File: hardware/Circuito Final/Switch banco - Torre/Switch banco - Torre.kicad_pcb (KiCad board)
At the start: 2 copper layers, 98.6 x 49 mm, 60 parts, among them J1 Conn_01x07, J2 Conn_02x07_Odd_Even, J3 Conn_01x07, Q1 MMBFJ112, Q1_1 MMBT2222A, Q3 MMBT2222A, U1 74HC595, U2 74HC4051

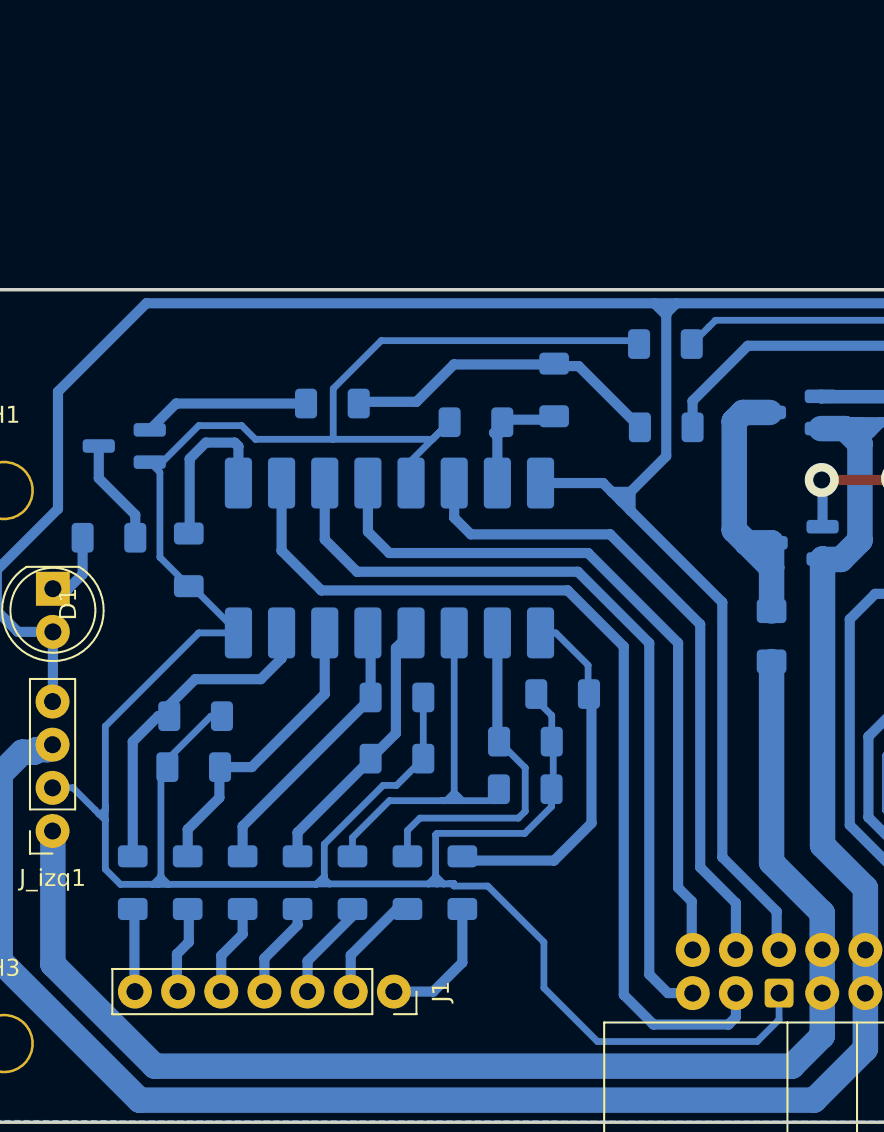
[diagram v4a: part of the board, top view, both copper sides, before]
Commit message: comienza arreglo de huellas
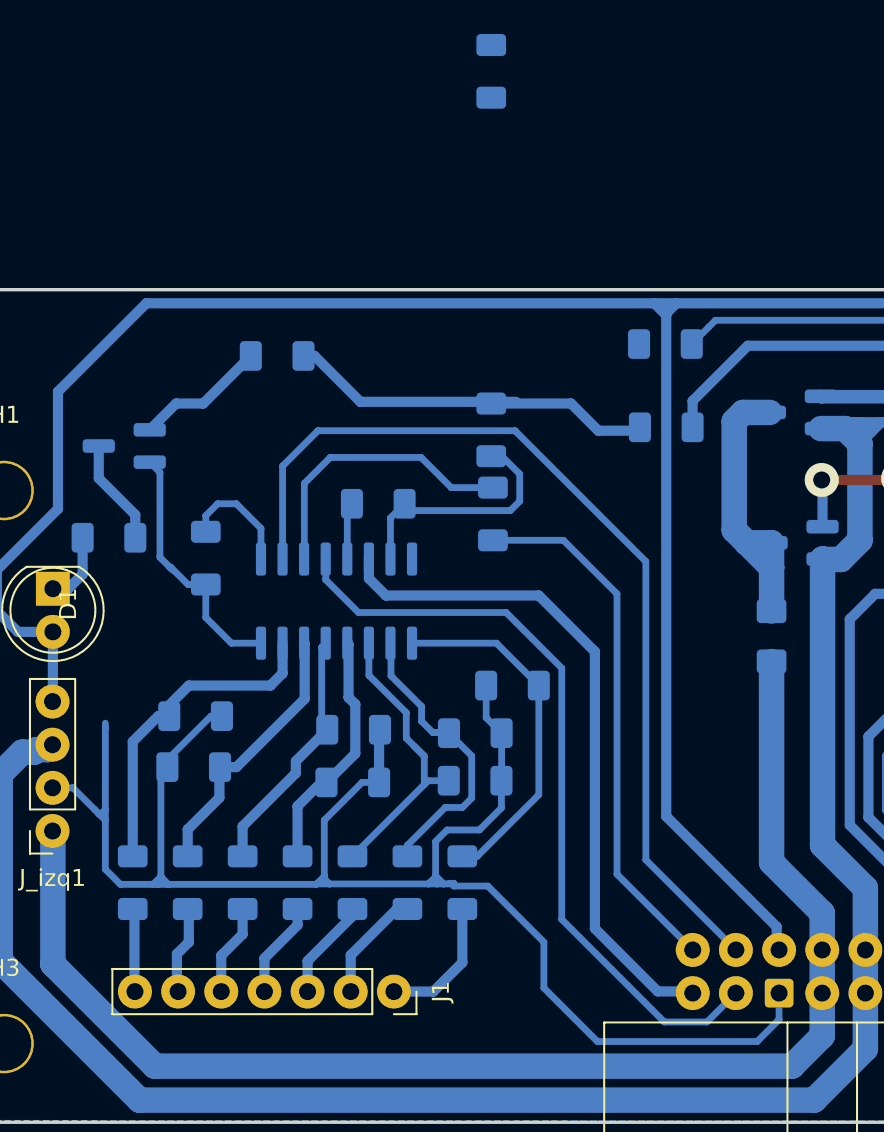
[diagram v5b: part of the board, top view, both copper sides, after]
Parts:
- added R2_11: 0, Resistor_SMD:R_1206_3216Metric_Pad1.30x1.75mm_HandSolder, B.Cu at (131.6, 88.4)
- added R2_12: 0, Resistor_SMD:R_1206_3216Metric_Pad1.30x1.75mm_HandSolder, B.Cu at (131.5, 62.4)
- U1: footprint Package_DIP:DIP-16_W7.62mm_SMDSocket_SmallPads -> Package_SO:SOIC-16_3.9x9.9mm_P1.27mm
- moved Rp1 7.49 mm to (124.9, 87.8)
- moved Rs0 4.38 mm to (131.5, 83.5)
- moved R4 4.29 mm to (118.9, 79.1)
- moved U1 4.02 mm to (122.4, 93.6)
- moved Rp6 3.18 mm to (123.4, 101.1)
- moved Rp4 2.99 mm to (130.6, 104.1)
- moved Rp2 2.99 mm to (132.8, 98.5)
- moved Rp3 2.99 mm to (130.6, 101.3)
- moved Rp5 2.95 mm to (123.4, 104.2)
- moved Rp9 1.00 mm to (114.7, 91.0)
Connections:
- J2 pad 11: /DATA -> /reset
- J2 pad 12: /reset -> /latch
- J2 pad 13: /latch -> /clock
- J2 pad 14: /clock -> /DATA
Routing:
- net GND: track 342.3 -> 288.0 mm
- net /Vcc: track 196.6 -> 187.0 mm
- net Net-(U1-QA): track 9.24 -> 14.5 mm
- net Net-(U1-QD): track 23.2 -> 18.5 mm
- net /Vbanco: track 19.1 -> 23.1 mm
- net /latch: track 42.3 -> 45.5 mm
- net Net-(U1-QH'): track 9.96 -> 6.89 mm
- net Net-(U1-QC): track 20.1 -> 17.2 mm
- net Net-(Q3-B): track 9.84 -> 7.75 mm
- net Net-(U1-QG): track 17.6 -> 16.0 mm
- net Net-(U1-QE): track 15.9 -> 14.3 mm
- net Net-(U1-QF): track 16.3 -> 14.8 mm
- net /DATA: track 39.2 -> 40.4 mm

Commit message: pruebas del shift register
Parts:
- removed Rp9: 10k, Resistor_SMD:R_1206_3216Metric_Pad1.30x1.75mm_HandSolder
- removed Rs0: 330, Resistor_SMD:R_1206_3216Metric_Pad1.30x1.75mm_HandSolder
- added C1: 100n, Capacitor_SMD:C_1206_3216Metric_Pad1.33x1.80mm_HandSolder, B.Cu at (130.6, 92.9)
- added C2: 100n, Capacitor_SMD:C_1206_3216Metric_Pad1.33x1.80mm_HandSolder, B.Cu at (175.1, 97.3)
- added Rs8: 330, Resistor_SMD:R_1206_3216Metric_Pad1.30x1.75mm_HandSolder, B.Cu at (128.6, 80.9)
- U2: footprint Package_DIP:DIP-16_W7.62mm_SMDSocket_SmallPads -> Package_SO:SOIC-16_3.9x9.9mm_P1.27mm
- moved R2_12 27.4 mm to (136.1, 89.4), turned to 0 degrees
- moved R2_9 23.2 mm to (173.0, 90.3), turned to 90 degrees
- moved R2_7 16.4 mm to (179.8, 100.2), turned to 90 degrees
- moved R2_2 8.69 mm to (177.6, 92.1), turned to 90 degrees
- moved R2_10 5.75 mm to (136.1, 79.5)
- moved R9 5.70 mm to (136.1, 83.2)
- moved R2_11 4.86 mm to (136.0, 86.4), turned to 180 degrees
- moved R2_4 4.36 mm to (177.0, 106.0)
- moved R4 4.16 mm to (122.7, 80.8), turned to -90 degrees
- moved R2_5 4.07 mm to (168.7, 110.8), turned to 0 degrees
- moved R1_1 3.09 mm to (185.0, 92.2)
- moved R1_2 3.05 mm to (185.0, 95.2)
- moved Rp1 2.37 mm to (122.8, 86.7)
- moved Q3 2.25 mm to (112.2, 84.4)
- moved R5 2.16 mm to (110.8, 88.6)
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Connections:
- J2 pad 11: /reset -> Net-(J2-Pin_11)
- J2 pad 12: /latch -> /reset
- J2 pad 13: /clock -> /Vcc
- J2 pad 9: /Vcc -> Net-(J2-Pin_9)
- R1_1 pad 2: /cell_neg5 -> /cell_neg6
- R1_2 pad 2: /cell_neg6 -> /cell_neg5
- R2_11 pad 1: /clock -> Net-(J2-Pin_9)
- R2_12 pad 2: /latch -> Net-(J2-Pin_11)
- U1 pad 10: /reset -> /Vcc
- U1 pad 9: Net-(U1-QH') -> unconnected-(U1-QH'-Pad9)
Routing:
- net /reset: track 56.0 -> 0.00 mm
- net GND: track 288.0 -> 251.4 mm
- net Net-(J2-Pin_9): track 0.00 -> 33.3 mm
- net Net-(J2-Pin_11): track 0.00 -> 29.6 mm
- net /latch: track 45.5 -> 19.5 mm
- net /Vcc: track 187.0 -> 205.5 mm
- net /Vbanco: track 23.1 -> 13.4 mm
- net Net-(U1-QA): track 14.5 -> 4.92 mm
- net Net-(Q1_1-B): track 35.0 -> 43.1 mm
- net /clock: track 48.3 -> 40.4 mm
- net /Bit_2: track 28.8 -> 21.1 mm
- net Net-(U2-A2): track 24.4 -> 17.4 mm
- net Net-(U1-QH'): track 6.89 -> 0.00 mm
- net Net-(U2-A5): track 28.0 -> 32.4 mm
- net Net-(U2-A7): track 24.1 -> 20.2 mm
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
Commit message: Sube version 2.1 del banco
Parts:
- added R2_13: 0, Resistor_SMD:R_1206_3216Metric_Pad1.30x1.75mm_HandSolder, B.Cu at (117.1, 86.2)
- added R2_14: 0, Resistor_SMD:R_1206_3216Metric_Pad1.30x1.75mm_HandSolder, B.Cu at (136.1, 79.9)
- moved R2_12 58.6 mm to (193.6, 78.3)
- moved C1 7.91 mm to (124.8, 87.5), turned to 180 degrees
- moved R2_10 6.14 mm to (142.1, 80.8), turned to 90 degrees
- moved Q3 5.43 mm to (117.1, 82.1)
- moved R5 4.58 mm to (110.1, 84.1), turned to 90 degrees
- moved R2_5 4.58 mm to (168.5, 115.4)
- moved R2_8 4.40 mm to (168.6, 118.3)
- moved Rp1 3.55 mm to (124.7, 83.8)
- moved R4 2.10 mm to (124.8, 80.5), turned to 180 degrees
- moved Rs8 1.98 mm to (130.0, 82.2)
- moved R2_11 1.80 mm to (134.6, 87.5)
- moved R9 0.43 mm to (136.2, 82.8)
- moved C2 0.43 mm to (175.5, 97.2)
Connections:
- J2 pad 11: Net-(J2-Pin_11) -> /clock
- J2 pad 12: /reset -> /latch
- J2 pad 9: Net-(J2-Pin_9) -> GND
- R2_11 pad 1: Net-(J2-Pin_9) -> /Vcc
- R2_11 pad 2: /clock -> /Vcc
- R2_12 pad 1: /latch -> GND
- R2_12 pad 2: Net-(J2-Pin_11) -> GND
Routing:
- net GND: track 251.4 -> 418.7 mm
- net Net-(J2-Pin_9): track 33.3 -> 0.00 mm
- net Net-(J2-Pin_11): track 29.6 -> 0.00 mm
- net /latch: track 19.5 -> 48.4 mm
- net /clock: track 40.4 -> 68.2 mm
- net /Vcc: track 205.5 -> 229.8 mm
- net Net-(U1-QA): track 4.92 -> 11.9 mm
- net Net-(U2-A5): track 32.4 -> 37.3 mm
- net Net-(Q3-B): track 9.20 -> 4.92 mm
- net /Vbanco: track 13.4 -> 9.25 mm
- net /salida_adc: track 33.3 -> 37.3 mm
- net Net-(D1-K): track 6.87 -> 10.5 mm
- net Net-(U2-A6): track 21.7 -> 22.8 mm
- net Net-(U2-A4): track 15.2 -> 15.9 mm
- net /Bit_2: track 21.1 -> 21.9 mm
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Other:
- board text added: "Balanceitor Banco v2.1"
- board text removed: "Balanceitor Banco v2.0"

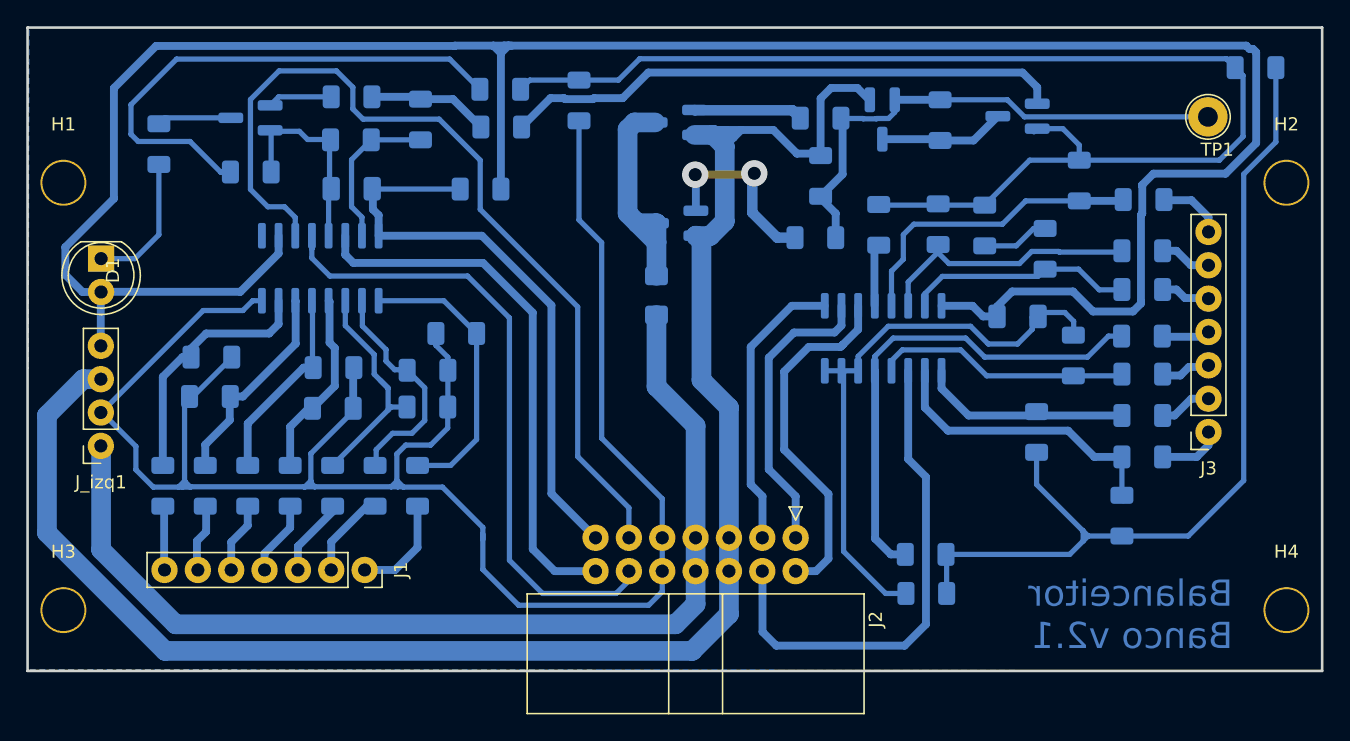
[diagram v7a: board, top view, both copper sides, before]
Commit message: agrego test points en el banco
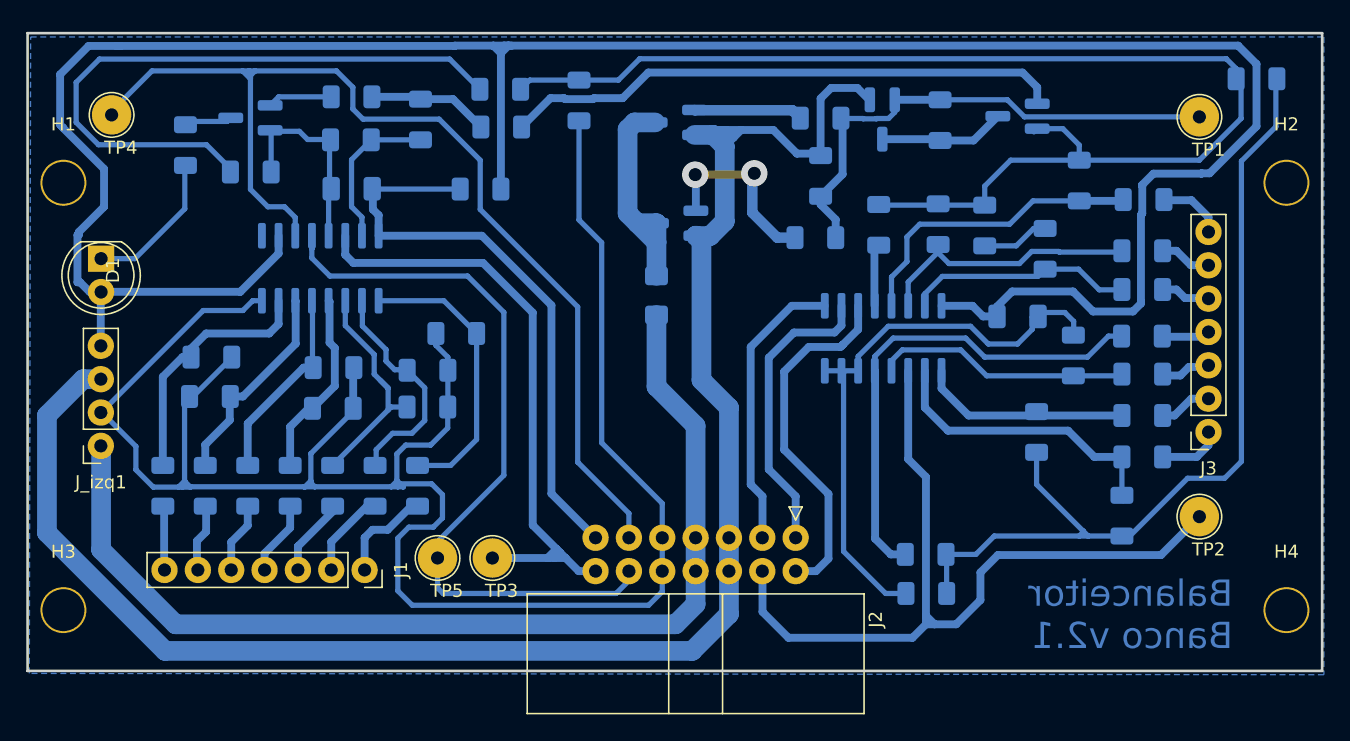
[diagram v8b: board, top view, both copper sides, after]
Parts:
- added TP2: TestPoint, TestPoint:TestPoint_Loop_D2.54mm_Drill1.5mm_Beaded, F.Cu at (189.4, 112.5)
- added TP3: TestPoint, TestPoint:TestPoint_Loop_D2.54mm_Drill1.5mm_Beaded, F.Cu at (135.5, 115.6)
- added TP4: TestPoint, TestPoint:TestPoint_Loop_D2.54mm_Drill1.5mm_Beaded, F.Cu at (106.5, 81.9)
- added TP5: TestPoint, TestPoint:TestPoint_Loop_D2.54mm_Drill1.5mm_Beaded, F.Cu at (131.3, 115.6)
- moved R5 2.03 mm to (112.1, 84.2)
- moved R2_12 0.85 mm to (193.7, 79.1)
- moved TP1 0.65 mm to (189.4, 82.0)
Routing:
- net /salida_adc: track 37.3 -> 62.9 mm
- net /clock: track 68.2 -> 83.5 mm
- net GND: track 418.7 -> 433.7 mm
- net /latch: track 48.4 -> 57.0 mm
- net /DATA: track 41.6 -> 47.8 mm
- net /Vcc: track 229.8 -> 233.7 mm
- net Net-(Q3-C): track 5.66 -> 3.44 mm
- net Net-(D1-K): track 10.5 -> 11.3 mm
- net Net-(Q1-S): track 40.1 -> 39.5 mm
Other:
- board size 98.6 x 49 mm -> 98.6 x 48.6 mm
